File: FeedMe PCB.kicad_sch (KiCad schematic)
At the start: 25 parts, among them J1 Battery In (12V), J2 Solar Charger In, J3 E-Paper Display, J4 Seeed Studio Xiao ESP32-C6, J5 Motor Out, Q1 2N7002, Q2 AO3401A, U1 TPS562200

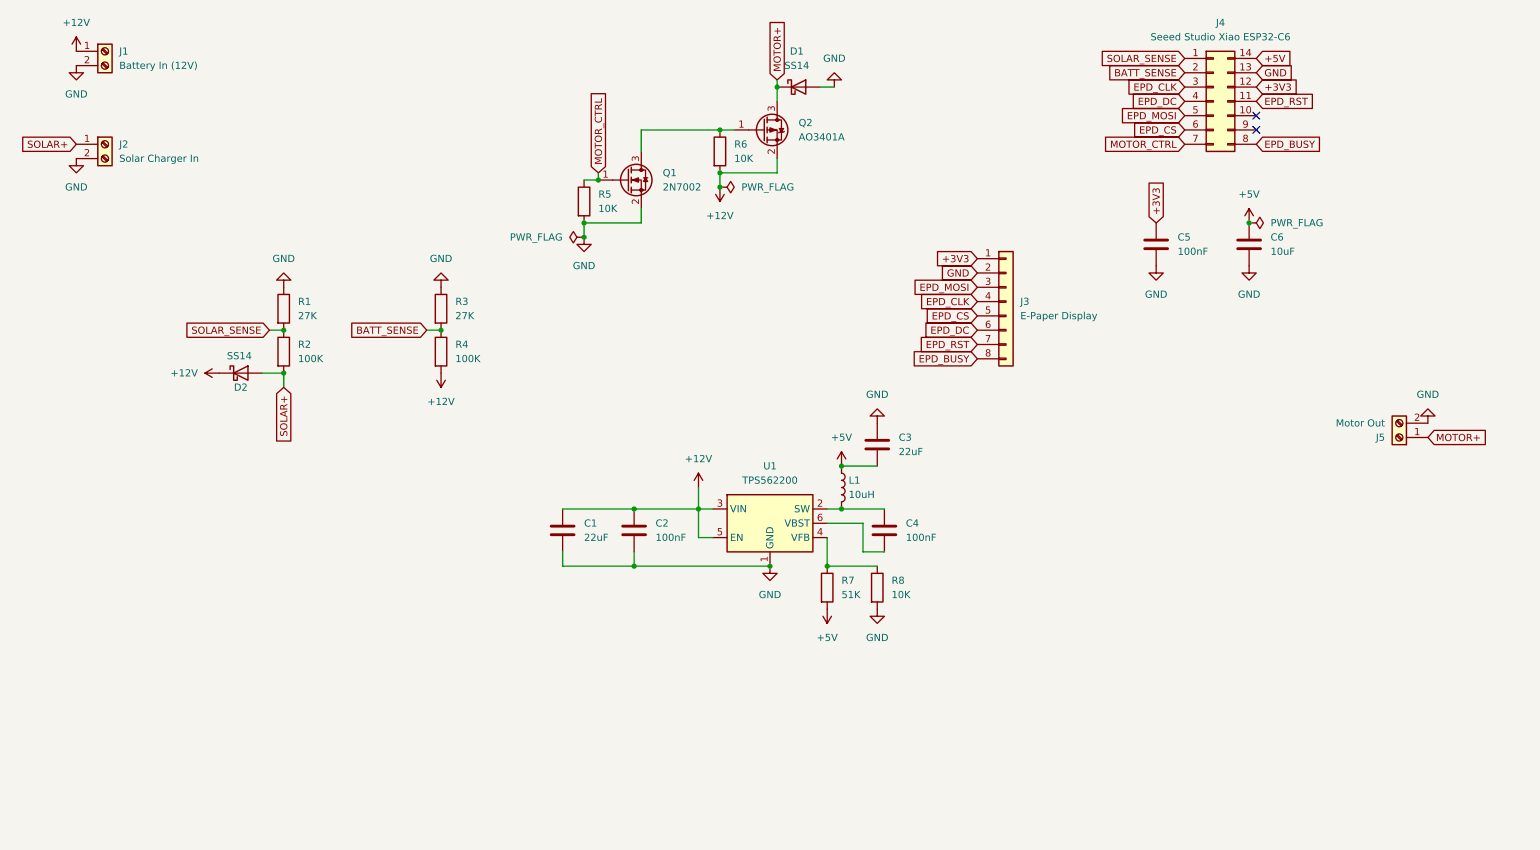
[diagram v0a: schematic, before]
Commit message: v0.1b - Buck-boost converter, pluggable terminals, reliability fixes
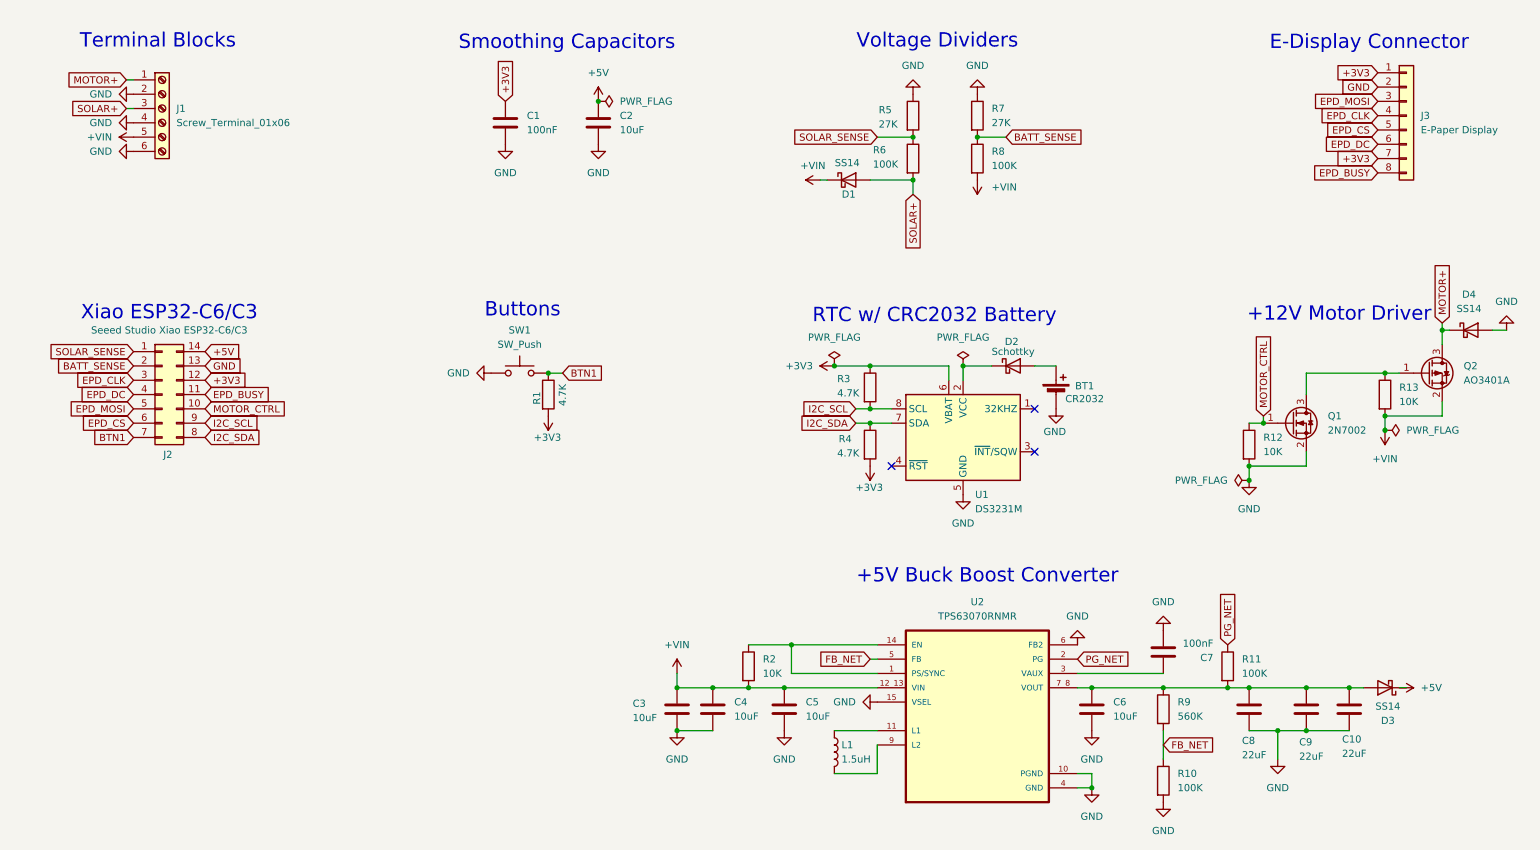
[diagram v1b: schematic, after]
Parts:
- removed J1: Battery In (12V), TerminalBlock_Phoenix:TerminalBlock_Phoenix_MKDS-1,5-2_1x02_P5.00mm_Horizontal, symbol Connector:Screw_Terminal_01x02
- removed J2: Solar Charger In, TerminalBlock_Phoenix:TerminalBlock_Phoenix_MKDS-1,5-2_1x02_P5.00mm_Horizontal, symbol Connector:Screw_Terminal_01x02
- removed J5: Motor Out, TerminalBlock_Phoenix:TerminalBlock_Phoenix_MKDS-1,5-2_1x02_P5.00mm_Horizontal, symbol Connector:Screw_Terminal_01x02
- removed R7: 51K, Resistor_SMD:R_0805_2012Metric, symbol Device:R
- removed R8: 10K, Resistor_SMD:R_0805_2012Metric, symbol Device:R
- removed U1: TPS562200, Package_TO_SOT_SMD:SOT-23-6, symbol Regulator_Switching:TPS562200
- added BT1: CR2032, Battery:BatteryHolder_Keystone_3034_1x20mm, symbol Device:Battery_Cell
- added C10, C9: 22uF, Capacitor_SMD:C_1206_3216Metric_Pad1.33x1.80mm_HandSolder, symbol Device:C
- added C5, C6: 10uF, Capacitor_SMD:C_1206_3216Metric_Pad1.33x1.80mm_HandSolder, symbol Device:C
- added D2: Schottky, Diode_SMD:D_SOD-123, symbol Device:D_Schottky
- added D3: SS14, Diode_SMD:D_SMA_Handsoldering, symbol Diode:SS14
- added J1: Screw_Terminal_01x06, Connector_Phoenix_MSTB:PhoenixContact_MSTBVA_2,5_6-G-5,08_1x06_P5.08mm_Vertical, symbol Connector:Screw_Terminal_01x06
- added R1, R3, R4: 4.7K, Resistor_SMD:R_0805_2012Metric_Pad1.20x1.40mm_HandSolder, symbol Device:R
- added R10, R11: 100K, Resistor_SMD:R_0805_2012Metric_Pad1.20x1.40mm_HandSolder, symbol Device:R
- added R2: 10K, Resistor_SMD:R_0805_2012Metric_Pad1.20x1.40mm_HandSolder, symbol Device:R
- added R9: 560K, Resistor_SMD:R_0805_2012Metric_Pad1.20x1.40mm_HandSolder, symbol Device:R
- added SW1: SW_Push, Button_Switch_SMD:SW_SPST_TL3342, symbol Switch:SW_Push
- added U1: DS3231M, Package_SO:SOIC-8_3.9x4.9mm_P1.27mm, symbol Timer_RTC:DS3231MZ
- added U2: TPS63070RNMR, Footprints:VREG_TPS63070RNMR, symbol Custom Symbols:TPS63070RNMR
- C1: renamed from C5; footprint Capacitor_SMD:C_0805_2012Metric -> Capacitor_SMD:C_0805_2012Metric_Pad1.18x1.45mm_HandSolder
- C2: renamed from C6; footprint Capacitor_SMD:C_0805_2012Metric -> Capacitor_SMD:C_0805_2012Metric_Pad1.18x1.45mm_HandSolder
- C3: renamed from C1; value 22uF -> 10uF; footprint Capacitor_SMD:C_1206_3216Metric -> Capacitor_SMD:C_1206_3216Metric_Pad1.33x1.80mm_HandSolder
- C4: value 100nF -> 10uF; footprint Capacitor_SMD:C_0805_2012Metric -> Capacitor_SMD:C_1206_3216Metric_Pad1.33x1.80mm_HandSolder
- C7: renamed from C2; footprint Capacitor_SMD:C_0805_2012Metric -> Capacitor_SMD:C_0805_2012Metric_Pad1.18x1.45mm_HandSolder
- C8: renamed from C3; footprint Capacitor_SMD:C_1206_3216Metric -> Capacitor_SMD:C_1206_3216Metric_Pad1.33x1.80mm_HandSolder
- D1: renamed from D2; footprint Diode_SMD:D_SMA -> Diode_SMD:D_SMA_Handsoldering
- D4: renamed from D1; footprint Diode_SMD:D_SMA -> Diode_SMD:D_SMA_Handsoldering
- J2: renamed from J4; value Seeed Studio Xiao ESP32-C6 -> Seeed Studio Xiao ESP32-C6/C3; footprint RF_Module:MCU_Seeed_ESP32C3 -> Footprints:MCU_Seeed_Xiao_ESP32C6_Through_Hole
- J3: footprint Connector_JST:JST_PH_B8B-PH-K_1x08_P2.00mm_Vertical -> Connector_JST:JST_PH_S8B-PH-K_1x08_P2.00mm_Horizontal
- L1: value 10uH -> 1.5uH; footprint Inductor_SMD:L_Bourns_SRN6045TA -> Inductor_SMD:L_Coilcraft_XAL4030-XXX
- R12: renamed from R5; footprint Resistor_SMD:R_0805_2012Metric -> Resistor_SMD:R_0805_2012Metric_Pad1.20x1.40mm_HandSolder
- R13: renamed from R6; footprint Resistor_SMD:R_0805_2012Metric -> Resistor_SMD:R_0805_2012Metric_Pad1.20x1.40mm_HandSolder
- R5: renamed from R1; footprint Resistor_SMD:R_0805_2012Metric -> Resistor_SMD:R_0805_2012Metric_Pad1.20x1.40mm_HandSolder
- R6: renamed from R2; footprint Resistor_SMD:R_0805_2012Metric -> Resistor_SMD:R_0805_2012Metric_Pad1.20x1.40mm_HandSolder
- R7: renamed from R3; footprint Resistor_SMD:R_0805_2012Metric -> Resistor_SMD:R_0805_2012Metric_Pad1.20x1.40mm_HandSolder
- R8: renamed from R4; footprint Resistor_SMD:R_0805_2012Metric -> Resistor_SMD:R_0805_2012Metric_Pad1.20x1.40mm_HandSolder
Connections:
- net +3V3: now also J3.7 (Pin_7), R1.2, R3.1, R4.2, U1.6 (VBAT)
- net +5V: now also D3.1 (K); no longer C8.2, L1.1
- net EPD_BUSY: now also J2.11 (Pin_11); no longer J2.8 (Pin_8)
- net GND: now also C4.2, C8.2, BT1.2 (-), C10.2, C5.2, C6.2, C9.2, J1.2 (Pin_2), J1.4 (Pin_4), J1.6 (Pin_6), R10.2, SW1.1, U1.5 (GND), U2.10 (PGND), U2.15 (VSEL), U2.4 (GND), U2.6 (FB2); no longer C8.1
- net MOTOR+: now also J1.1 (Pin_1)
- net MOTOR_CTRL: now also J2.10 (Pin_10); no longer J2.7 (Pin_7)
- net SOLAR+: now also J1.3 (Pin_3)
- net at L1.2: now also U2.9 (L2); no longer C4.1
- net I2C_SCL: now reaches J2.9 (Pin_9)
- net I2C_SCL: now also R3.2, U1.8 (SCL)
- net +12V renamed +VIN
- net +VIN: now also C4.1, C5.1, J1.5 (Pin_5), R2.2, U2.12_13 (VIN); no longer C7.1
- removed net EPD_RST: J2.11 (Pin_11), J3.7 (Pin_7)
- new net: C7.1, U2.3 (VAUX)
- new net: C10.1, C6.1, C8.1, C9.1, D3.2 (A), R11.2, R9.1, U2.7_8 (VOUT)
- new net: R2.1, U2.1 (PS/SYNC), U2.14 (EN)
- new net: L1.1, U2.11 (L1)
- new net: BT1.1 (+), D2.2 (A)
- new net: D2.1 (K), U1.2 (VCC)
- new net BTN1: J2.7 (Pin_7), R1.1, SW1.2
- new net FB_NET: R10.1, R9.2, U2.5 (FB)
- new net I2C_SDA: J2.8 (Pin_8), R4.1, U1.7 (SDA)
- new net PG_NET: R11.1, U2.2 (PG)
- no-connect marks 2 -> 3
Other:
- note added: "+12V Motor Driver"
- note added: "+5V Buck Boost Converter"
- note added: "Buttons"
- note added: "E-Display Connector"
- note added: "RTC w/ CRC2032 Battery"
- note added: "Smoothing Capacitors"
- note added: "Terminal Blocks"
- note added: "Voltage Dividers"
- note added: "Xiao ESP32-C6/C3"
- moved on the sheet: C1, C2, C3, C7, C8, D1, D4, J2, J3, Q1, Q2, R12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
